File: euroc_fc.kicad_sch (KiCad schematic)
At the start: 123 parts, among them J1 Micro-Fit, J10 USB_C_Receptacle_USB2.0, J2 Micro-Fit, J3 Micro-Fit, J4 SMA, J5 JST-GH, J6 JST-GH, J7 JST-GH, J8 JST-GH, J9 Micro_SD_Card_Det, Q1 DMG2302U, Q2 AOSP21321, Q3 DMG2302U, Q4 AOSP21321, Q5 DMG2302U, Q6 DMG2302U, Q7 DMG2302U, SW1 EVQ-PUC02K, SW2 EVQ-PUC02K, U1 STM32F401RCT6, U10 Ai-Thinker-Ra-01, U11 W25Q256JVF, U2 L7805, U3 L7805, U4 AZ1117I-3.3, U5 LSM6DSR, U6 ADXL375, U7 MS5611-01BA, U8 BMM150, U9 SAM-M8Q, Y1 25M

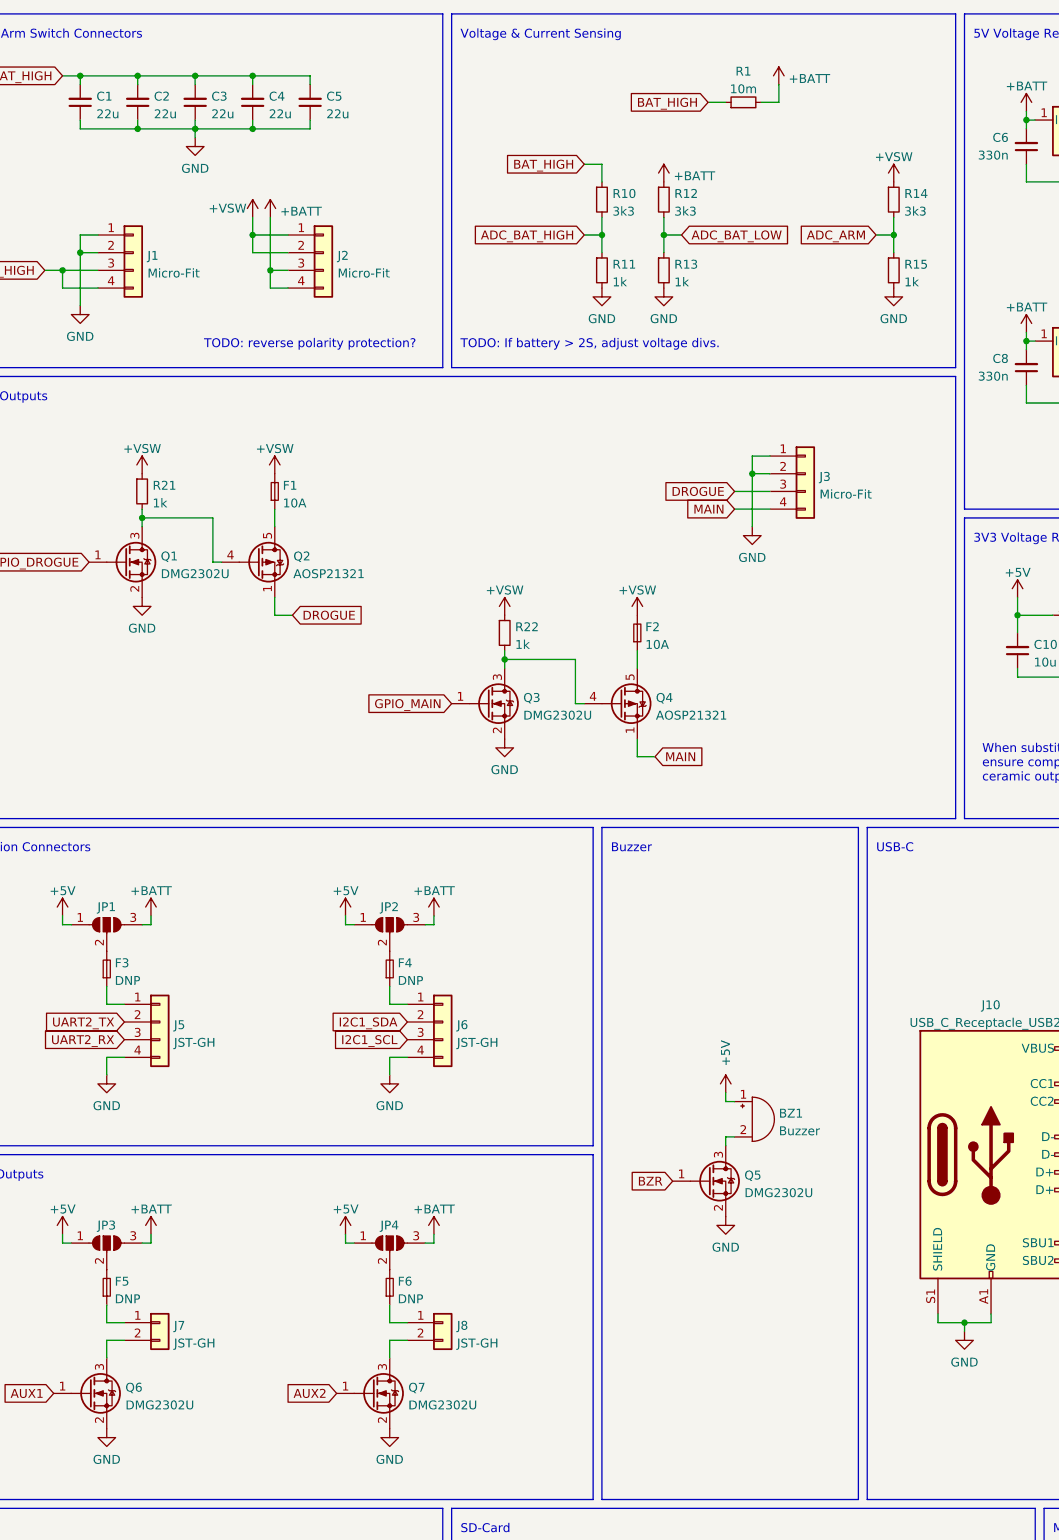
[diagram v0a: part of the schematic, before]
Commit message: Update part selection, complete BOM
- Voltage divider reduced to 1k / (1k + 1k8)
- Diode changed to onsemi SS26FL (higher current capacity)
- N-Ch. MOSFET changed to DMN2056U (official successor)
- uSD holder changed to Hirose DM3AT (push-push)
- Vendor and Datasheet fields filled out for (almost) all components
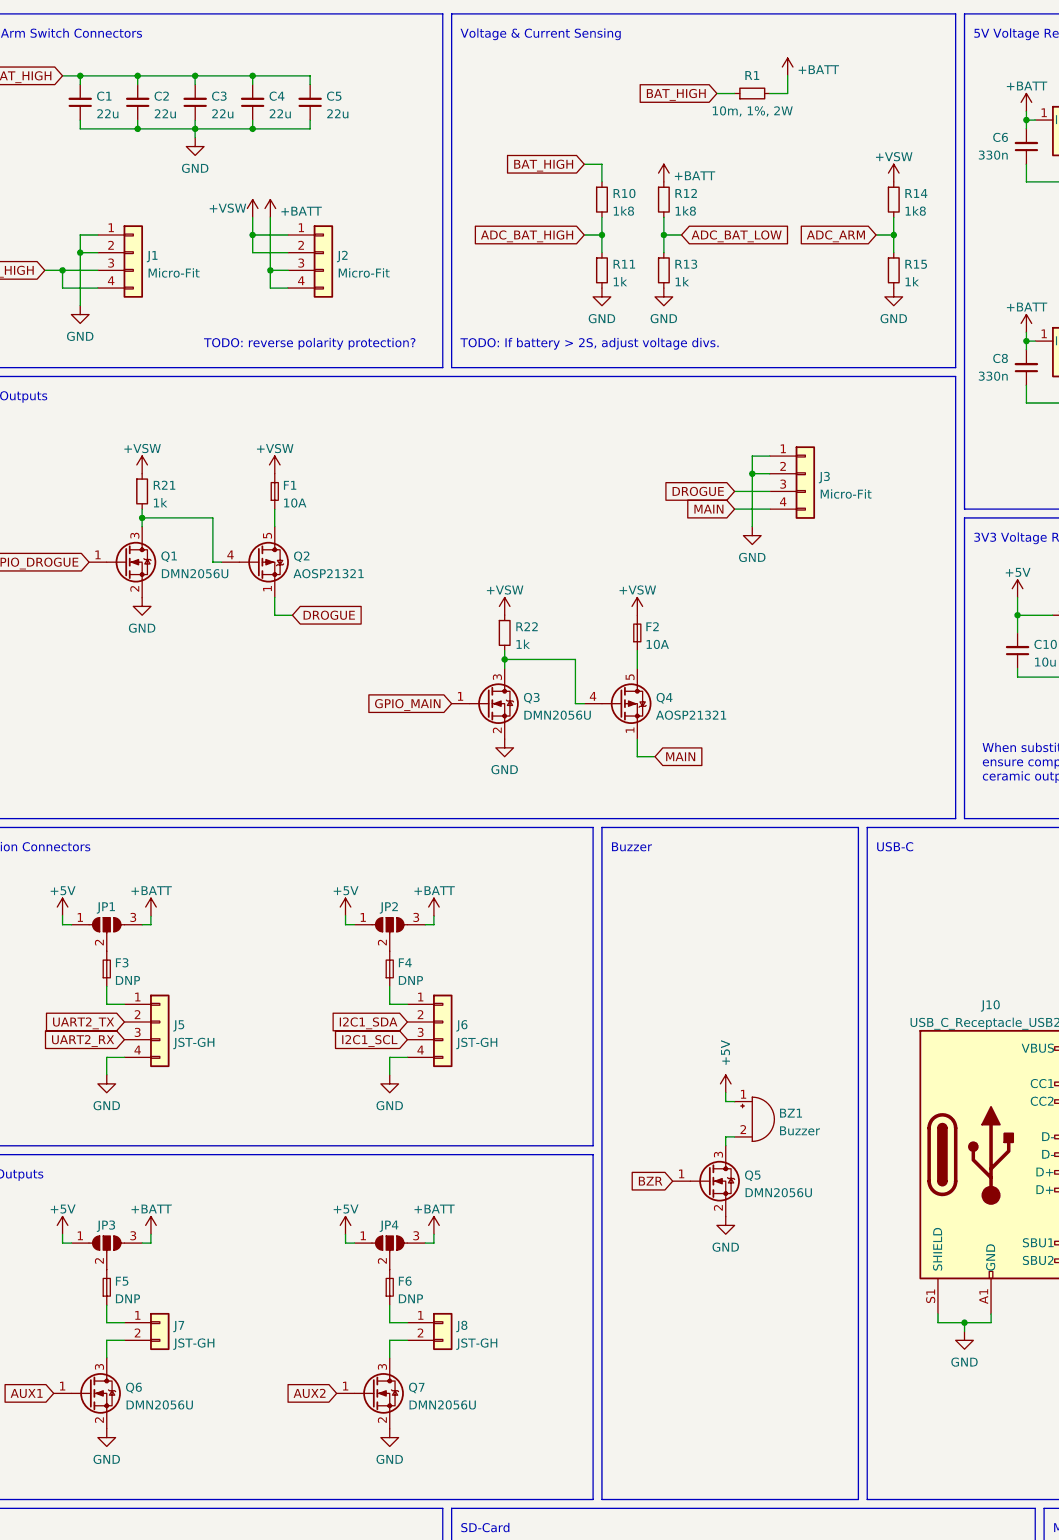
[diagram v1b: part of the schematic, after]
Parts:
- C1, C10, C11, C12, C13, C14, C15, C16, C17, C18, C19, C2, C20, C21, C22, C23, C24, C25, C26, C27, C28, C29, C3, C30, C31, C32, C33, C36, C37, C38, C39, C4, C5, C6, C7, C8, C9: Vendor (none) -> https://www.lcsc.com/product-detail/Multilayer-Ceramic-Capa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
- C34, C35, F3, F4, F5, F6: Vendor (none) -> N/A
- D1, D2, D3: value DSS16UTR -> SS26FL; Vendor (none) -> https://www.digikey.de/de/products/detail/onsemi/SS26FL/530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
- D4, D5, D6, D7, D8: Vendor (none) -> https://www.digikey.de/de/products/detail/osram-opto-semico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
- J1, J2, J3: Notes (none) -> Housing: 430250400, Crimp Terminals: 430300001; Vendor (none) -> https://www.lcsc.com/product-detail/Wire-To-Board-Wire-To-W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
- J4: Vendor (none) -> https://www.digikey.de/de/products/detail/te-connectivity-a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
- J9: footprint Connector_Card:microSD_HC_Hirose_DM3D-SF -> Connector_Card:microSD_HC_Hirose_DM3AT-SF-PEJM5; Vendor (none) -> https://www.lcsc.com/product-detail/SD-Card-Connectors_HRS-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
- L1, L2, L3: Vendor https://www.digikey.de/de/products/detail/murata-electronic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 -> https://www.lcsc.com/product-detail/Ferrite-Beads_Murata-El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
- Q1, Q3, Q5, Q6, Q7: value DMG2302U -> DMN2056U; Vendor (none) -> https://www.lcsc.com/product-detail/MOSFETs_Diodes-Incorpor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
- Q2, Q4: Vendor https://www.digikey.de/de/products/detail/alpha-omega-semic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 -> https://www.lcsc.com/product-detail/MOSFETs_Alpha-Omega-Sem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
- R1: value 10m -> 10m, 1%, 2W; Vendor (none) -> https://www.lcsc.com/product-detail/Current-Sense-Resistors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
- R10, R12, R14: value 3k3 -> 1k8; Vendor (none) -> https://www.lcsc.com/product-detail/Chip-Resistor-Surface-M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
- R11, R13, R15, R16, R17, R18, R19, R2, R20, R21, R22, R3, R4, R5, R6, R7, R8, R9: Vendor (none) -> https://www.lcsc.com/product-detail/Chip-Resistor-Surface-M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
- SW1, SW2: Vendor https://www.digikey.de/de/products/detail/panasonic-electro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 -> https://www.lcsc.com/product-detail/Tactile-Switches_PANASO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
- U2, U3: Vendor (none) -> https://www.lcsc.com/product-detail/Linear-Voltage-Regulato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
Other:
- moved on the sheet: R1

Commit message: Tweak LoRa trans line impedance, power planes
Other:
- note added: "TODO: Add testpoint for reset and safeboot"
- note added: "TODO: rename nets to conform to STM32 nomenclature"
- note removed: "TODO: diode part selection (amps?)"
- note removed: "TODO: fill out datasheets, vendor, generate BOM"
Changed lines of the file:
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@@
-    (effects (font (size 1.27 1.27)) (justify left bottom))
-  )
-  (text "TODO: fill out datasheets, vendor, generate BOM" (at 252.73 309.88 0)
     (effects (font (size 1.27 1.27)) (justify left bottom))
   )
@@
     (effects (font (size 1.27 1.27)) (justify left bottom))
   )
-  (text "TODO: diode part selection (amps?)" (at 349.25 314.96 0)
-    (effects (font (size 1.27 1.27)) (justify left bottom))
-  )
   (text "Mounting Holes" (at 265.43 232.41 0)
     (effects (font (size 1.27 1.27)) (justify left bottom))
   )
   (text "Battery & Arm Switch Connectors" (at 105.41 17.78 0)
+    (effects (font (size 1.27 1.27)) (justify left bottom))
+  )
+  (text "TODO: rename nets to conform to STM32 nomenclature"
+    (at 359.41 213.36 0)
     (effects (font (size 1.27 1.27)) (justify left bottom))
   )
@@
     (effects (font (size 1.27 1.27)) (justify left bottom))
   )
+  (text "TODO: Add testpoint for reset and safeboot" (at 17.78 224.79 0)
+    (effects (font (size 1.27 1.27)) (justify left bottom))
+  )

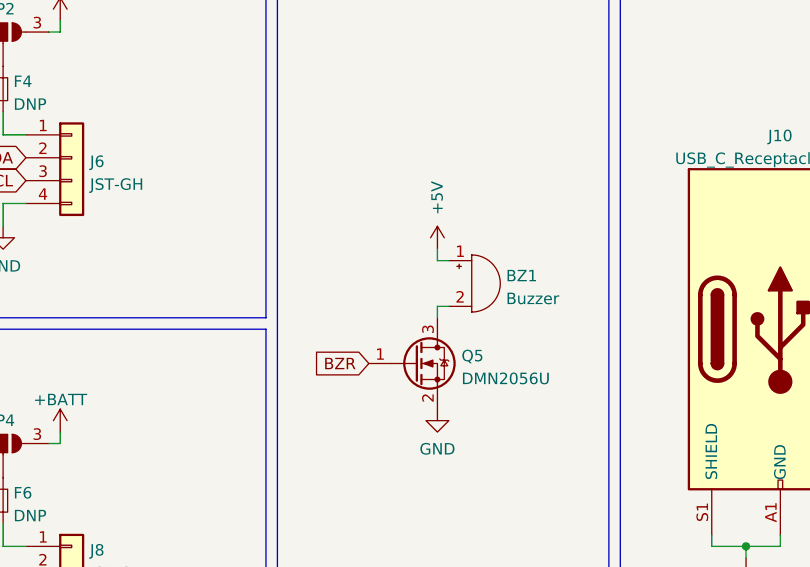
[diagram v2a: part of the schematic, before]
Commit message: Add flyback diode for buzzer
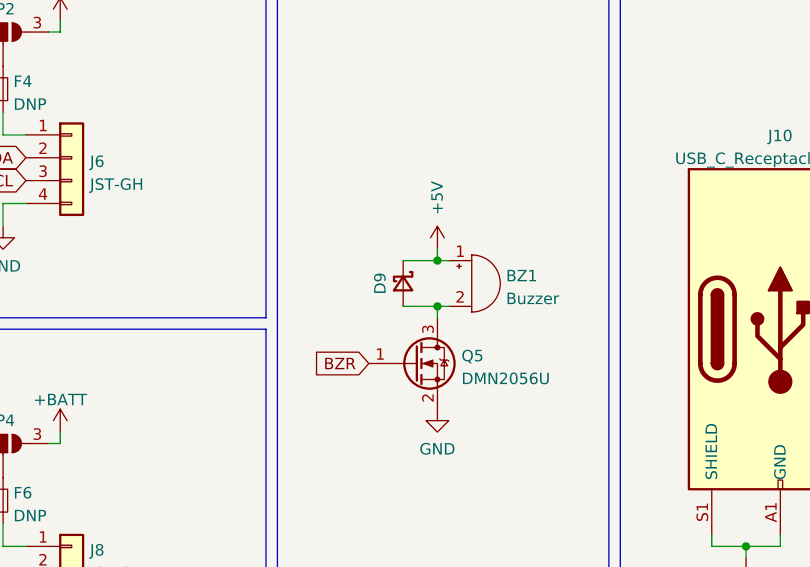
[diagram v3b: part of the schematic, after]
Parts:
- added D9: SS26FL, Diode_SMD:D_SOD-123F, symbol Device:D_Schottky_Small
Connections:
- net +5V: now also D9.1 (K)
- net at BZ1.2 (+), Q5.3 (D): now also D9.2 (A)
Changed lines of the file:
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@@
   (junction (at 142.24 22.86) (diameter 0) (color 0 0 0 0)
   )
+  (junction (at 218.44 175.26) (diameter 0) (color 0 0 0 0)
+  )
   (junction (at 153.035 50.8) (diameter 0) (color 0 0 0 0)
   )
@@
   (junction (at 270.51 38.1) (diameter 0) (color 0 0 0 0)
   )
+  (junction (at 218.44 170.18) (diameter 0) (color 0 0 0 0)
+  )
   (junction (at 331.47 39.37) (diameter 0) (color 0 0 0 0)
   )
@@
     (stroke (width 0) (type default) (color 0 0 0 0))
   )
+  (wire (pts (xy 214.63 170.18) (xy 218.44 170.18))
+    (stroke (width 0) (type default) (color 0 0 0 0))
+  )
   (wire (pts (xy 163.83 144.78) (xy 163.83 143.51))
     (stroke (width 0) (type default) (color 0 0 0 0))
@@
     (stroke (width 0) (type default) (color 0 0 0 0))
   )
+  (wire (pts (xy 214.63 175.26) (xy 218.44 175.26))
+    (stroke (width 0) (type default) (color 0 0 0 0))
+  )
   (polyline (pts (xy 199.39 177.8) (xy 199.39 227.33))
     (stroke (width 0) (type default) (color 0 0 0 0))
@@
     (pin "9")
   )
+  (symbol (lib_id "Device:D_Schottky_Small") (at 214.63 172.72 270) (unit 1)
+    (in_bom yes) (on_board yes)
+    (property "Reference" "D9" (id 0) (at 212.09 172.72 0))
+    (property "Value" "SS26FL" (id 1) (at 212.4511 172.466 0)
+      (effects (font (size 1.27 1.27)) hide)
+    )
+    (property "Footprint" "Diode_SMD:D_SOD-123F" (id 2) (at 214.63 172.72 90)
+      (effects (font (size 1.27 1.27)) hide)
+    )
+    (property "Datasheet" "https://www.onsemi.com/pdf/datasheet/ss26fl-d.pdf" (id 3) (at 214.63 172.72 90)
+      (effects (font (size 1.27 1.27)) hide)
+    )
+    (property "Vendor" "https://www.digikey.de/de/products/detail/onsemi/SS26FL/5305067" (id 4) (at 214.63 172.72 0)
+      (effects (font (size 1.27 1.27)) hide)
+    )
+    (pin "1")
+    (pin "2")
+  )
   (symbol (lib_id "power:+3V3") (at 375.285 66.04 90) (unit 1)
     (in_bom yes) (on_board yes)
@@
       (reference "D8") (unit 1) (value "green") (footprint "LED_SMD:LED_0603_1608Metric")
     )
+    (path "/107c8b80-df6b-44e0-b82a-ddfe98f13513"
+      (reference "D9") (unit 1) (value "SS26FL") (footprint "Diode_SMD:D_SOD-123F")
+    )
     (path "/3d12d597-4244-424e-8897-240a7879c795"

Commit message: Fix ADC pin assignment, rename nets
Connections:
- net ADC_BAT_HIGH: now also U1.25 (PC5); no longer U1.37 (PC6)
- net ADC_BAT_LOW: now also U1.24 (PC4); no longer U1.36 (PB15)
- net SPI1_CS_BARO: now also U1.37 (PC6); no longer U1.24 (PC4)
- net SPI2_MISO: now also U1.10 (PC2), U11.8 (DO(IO1)); no longer U1.52 (PC11), U6.12 (SDO/ADDR)
- net SPI2_MOSI: now also U1.11 (PC3), U11.15 (DI(IO0)); no longer U1.53 (PC12), U6.13 (SDA/SDI/SDIO)
- net SPI2_SCL: now also U1.34 (PB13), U11.16 (CLK); no longer U1.51 (PC10), U6.14 (SCL/SCLK)
- net SPI3_MISO: now also U1.52 (PC11), U6.12 (SDO/ADDR); no longer U1.10 (PC2), U11.8 (DO(IO1))
- net SPI3_MOSI: now also U1.53 (PC12), U6.13 (SDA/SDI/SDIO); no longer U1.11 (PC3), U11.15 (DI(IO0))
- net SPI3_SCL: now also U1.51 (PC10), U6.14 (SCL/SCLK); no longer U1.34 (PB13), U11.16 (CLK)
- net UART1_RX: now also J5.3 (Pin_3), U1.43 (PA10); no longer L3.2, U1.17 (PA3)
- net UART1_TX: now also J5.2 (Pin_2), U1.42 (PA9); no longer L2.2, U1.16 (PA2)
- net UART2_RX: now also L3.2, U1.17 (PA3); no longer J5.3 (Pin_3), U1.43 (PA10)
- net UART2_TX: now also L2.2, U1.16 (PA2); no longer J5.2 (Pin_2), U1.42 (PA9)
- net SPI2_CS_ACC2 renamed SPI3_CS_ACC2
- net SPI3_CS_FLASH renamed SPI2_CS_FLASH
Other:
- note added: "TODO: check ADC_BAT_HIGH/LOW"
- note removed: "TODO: rename nets to conform to STM32 nomenclature"

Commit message: Place additional test points
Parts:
- added TP10, TP11, TP12, TP13, TP14, TP15, TP16, TP17, TP18, TP19, TP20, TP21, TP22, TP23, TP4, TP5, TP6, TP7, TP8, TP9: TestPoint, TestPoint:TestPoint_Pad_D1.0mm, symbol Connector:TestPoint
- H1, H2, H3, H4, H5, H6, JP1, JP2, JP3, JP4, TP1, TP2, TP3: now left out of the parts list
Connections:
- net SPI1_CS_ACC1: now also TP7.1
- net SPI1_CS_BARO: now also TP9.1
- net SPI1_CS_MAG: now also TP8.1
- net SPI1_CS_RADIO: now also TP10.1
- net SPI1_CS_SD: now also TP11.1
- net SPI1_MISO: now also TP6.1
- net SPI1_MOSI: now also TP5.1
- net SPI1_SCL: now also TP4.1
- net SPI2_CS_FLASH: now also TP15.1
- net SPI2_MISO: now also TP14.1
- net SPI2_MOSI: now also TP13.1
- net SPI2_SCL: now also TP12.1
- net SPI3_CS_ACC2: now also TP19.1
- net SPI3_MISO: now also TP18.1
- net SPI3_MOSI: now also TP17.1
- net SPI3_SCL: now also TP16.1
- net UART2_RX: now also TP21.1
- net UART2_TX: now also TP20.1
- net GPS_RESET: now reaches U9.18 (~{RESET})
- net GPS_RESET: now also TP23.1
- net GPS_SAFEBOOT: now reaches U9.8 (~{SAFEBOOT})
- net GPS_SAFEBOOT: now also TP22.1
- no-connect marks 32 -> 30
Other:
- note added: "Test Points"
- moved on the sheet: BZ1, C31, C32, C33, D3, D9, J10, L2, L3, Q5, R16, R17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

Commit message: Remove various TODOs
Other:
- note removed: "TODO: Add testpoint for reset and safeboot"
- note removed: "TODO: beads really necessary?"
- note removed: "TODO: check ADC_BAT_HIGH/LOW"
- note removed: "TODO: do we need a GPS backup battery?"
- note removed: "TODO: double-check pin assignments"
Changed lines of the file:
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@@
-    (effects (font (size 1.27 1.27)) (justify left bottom))
-  )
-  (text "TODO: double-check pin assignments" (at 358.775 210.82 0)
     (effects (font (size 1.27 1.27)) (justify left bottom))
   )
@@
   )
   (text "TODO: can unused IO pins be left floating?" (at 129.54 272.415 0)
-    (effects (font (size 1.27 1.27)) (justify left bottom))
-  )
-  (text "TODO: do we need a GPS backup battery?" (at -34.29 212.09 0)
     (effects (font (size 1.27 1.27)) (justify left bottom))
   )
@@
     (effects (font (size 1.27 1.27)) (justify left bottom))
   )
-  (text "TODO: Add testpoint for reset and safeboot" (at -41.91 227.33 0)
-    (effects (font (size 1.27 1.27)) (justify left bottom))
-  )
   (text "IMU (Accelerometer & Gyroscope)" (at 15.24 17.78 0)
     (effects (font (size 1.27 1.27)) (justify left bottom))
@@
     (effects (font (size 1.27 1.27)) (justify left bottom))
   )
-  (text "TODO: beads really necessary?" (at -25.4 222.25 0)
-    (effects (font (size 1.27 1.27)) (justify left bottom))
-  )
   (text "TODO: reverse polarity protection?" (at 143.51 62.23 0)
     (effects (font (size 1.27 1.27)) (justify left bottom))
@@
     (effects (font (size 1.27 1.27)) (justify left bottom))
   )
-  (text "TODO: check ADC_BAT_HIGH/LOW" (at 370.84 199.39 0)
-    (effects (font (size 1.27 1.27)) (justify left bottom))
-  )
